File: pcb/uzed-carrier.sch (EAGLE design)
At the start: 11 parts

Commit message: finished with uZed carrier board.
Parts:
- added C1: 10uF, SparkFun-Capacitors:10UF-POLAR-EIA3216-16V-10%(TANT)
- added SJ1, SJ3: (no value), SparkFun-Retired:SOLDERJUMPER_2WAYS
- added UZEDLOWER, UZEDUPPER: (no value), SparkFun-Connectors:CONN_08X2
- renumbered J1 to 3V3_POWER/SPI, J2 to EXPOSURE_CTRL, J3 to 2V5_POWER
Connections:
- net CLK: now also UZEDUPPER.15
- net D0: now also UZEDUPPER.12
- net D1: now also UZEDUPPER.11
- net D2: now also UZEDUPPER.10
- net D3: now also UZEDUPPER.9
- net D4: now also UZEDUPPER.8
- net D5: now also UZEDUPPER.7
- net D6: now also UZEDUPPER.6
- net D7: now also UZEDUPPER.5
- net D8: now also UZEDUPPER.4
- net D9: now also UZEDUPPER.3
- net FRAME_VALID: now also UZEDLOWER.10
- net GND: now also C1.-, SJ1.3, SJ3.3, UZEDUPPER.1, UZEDUPPER.2
- net INT_TIME1: now also UZEDLOWER.11
- net INT_TIME2: now also UZEDLOWER.13
- net INT_TIME3: now also UZEDLOWER.15
- net LINE_VALID: now also UZEDLOWER.9
- net RESET: now also UZEDUPPER.16
- net SPI_CLK: now also UZEDLOWER.3
- net SPI_DATA: now also UZEDLOWER.5
- net SPI_EN: now also UZEDLOWER.1
- net VIN: now also C1.+, UZEDLOWER.7, UZEDLOWER.8
- net VRESET_1: now also SJ1.1, SJ3.1
- net VRESET_2: now also SJ1.2
- net VRESET_3: now also SJ3.2

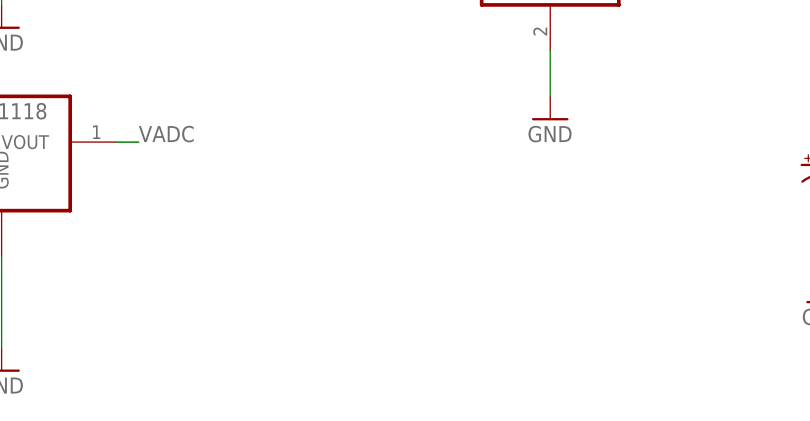
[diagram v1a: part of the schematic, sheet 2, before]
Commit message: added mosfet for fpga control of board power
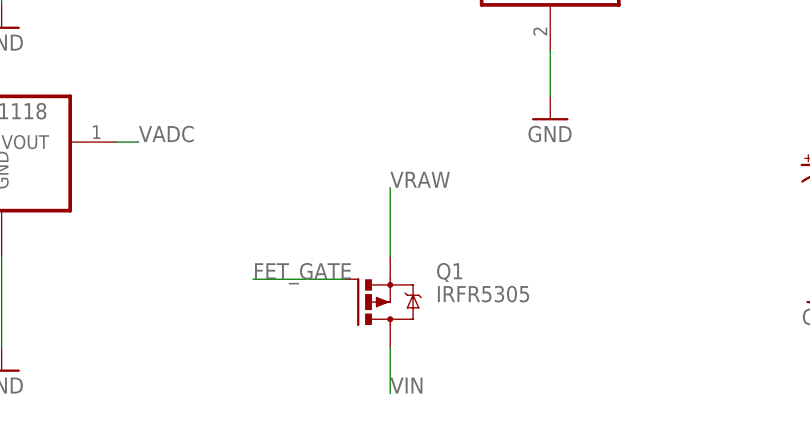
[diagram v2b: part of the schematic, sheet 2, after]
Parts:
- added Q1: IRFR5305, transistor-power:IRFR5305
- added R1: (no value), rcl:R-EU_M1206
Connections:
- new net FET_GATE: Q1.G, R1.2
- new net N$1: R1.1, UZEDLOWER.6
- new net VRAW: Q1.S, UZEDLOWER.7, UZEDLOWER.8
- net VIN: now also Q1.D; no longer UZEDLOWER.7, UZEDLOWER.8
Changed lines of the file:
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@@
 <part name="SUPPLY4" library="SparkFun-Aesthetics" deviceset="VIN" device=""/>
 <part name="GND7" library="SparkFun-Aesthetics" deviceset="GND" device=""/>
+<part name="Q1" library="transistor-power" library_urn="urn:adsk.eagle:library:400" deviceset="IRF?5305" device="R" package3d_urn="urn:adsk.eagle:package:29503/1"/>
+<part name="R1" library="rcl" library_urn="urn:adsk.eagle:library:334" deviceset="R-EU_" device="M1206" package3d_urn="urn:adsk.eagle:package:23566/1"/>
 </parts>
 <sheets>
@@
 <instance part="GND3" gate="1" x="111.76" y="30.48"/>
 <instance part="GND8" gate="1" x="154.94" y="30.48"/>
+<instance part="R1" gate="G$1" x="167.64" y="81.28"/>
 </instances>
 <busses>
@@
 </segment>
 </net>
-<net name="VIN" class="0">
+<net name="VRAW" class="0">
 <segment>
 <pinref part="UZEDLOWER" gate="G$1" pin="7"/>
@@
 <wire x1="147.32" y1="78.74" x2="152.4" y2="78.74" width="0.1524" layer="91"/>
 <label x="154.94" y="78.74" size="1.778" layer="95"/>
+</segment>
+</net>
+<net name="FET_GATE" class="0">
+<segment>
+<pinref part="R1" gate="G$1" pin="2"/>
+<wire x1="172.72" y1="81.28" x2="177.8" y2="81.28" width="0.1524" layer="91"/>
+<label x="177.8" y="81.28" size="1.778" layer="95"/>
+</segment>
+</net>
+<net name="N$1" class="0">
+<segment>
+<pinref part="R1" gate="G$1" pin="1"/>
+<pinref part="UZEDLOWER" gate="G$1" pin="6"/>
+<wire x1="162.56" y1="81.28" x2="147.32" y2="81.28" width="0.1524" layer="91"/>
 </segment>
 </net>
@@
 <instance part="SUPPLY4" gate="G$1" x="104.14" y="35.56"/>
 <instance part="GND7" gate="1" x="104.14" y="12.7"/>
+<instance part="Q1" gate="G$1" x="53.34" y="12.7"/>
 </instances>
 <busses>
@@
 <pinref part="SUPPLY4" gate="G$1" pin="VIN"/>
 </segment>
+<segment>
+<pinref part="Q1" gate="G$1" pin="D"/>
+<wire x1="55.88" y1="7.62" x2="55.88" y2="2.54" width="0.1524" layer="91"/>
+<label x="55.88" y="2.54" size="1.778" layer="95"/>
+</segment>
 </net>
 <net name="GND" class="0">
@@
 </segment>
 </net>
+<net name="VRAW" class="0">
+<segment>
+<pinref part="Q1" gate="G$1" pin="S"/>
+<wire x1="55.88" y1="17.78" x2="55.88" y2="25.4" width="0.1524" layer="91"/>
+<label x="55.88" y="25.4" size="1.778" layer="95"/>
+</segment>
+</net>
+<net name="FET_GATE" class="0">
+<segment>
+<pinref part="Q1" gate="G$1" pin="G"/>
+<wire x1="50.8" y1="15.24" x2="40.64" y2="15.24" width="0.1524" layer="91"/>
+<label x="40.64" y="15.24" size="1.778" layer="95"/>
+</segment>
+</net>
